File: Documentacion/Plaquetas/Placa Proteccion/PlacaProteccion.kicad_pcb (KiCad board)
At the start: 2 copper layers, 100 x 50 mm, 18 parts, among them J1 POW_IN, J2 POW_OUT, J3 RELAY_CTRL, J4 RELAY_SW, K1 Modulo_Relé, Q1 IRF4905, SW1 ON_SW, SW2 OFF_SW, U1 LM2903, U6 TL431LP

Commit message: Protection PCB footprint update, adjustable zenner ref set, pad resize
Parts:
- added R3: 100k, Resistor_THT:R_Axial_DIN0309_L9.0mm_D3.2mm_P12.70mm_Horizontal, F.Cu at (81.3, 59.5)
- added R4: 100k, Resistor_THT:R_Axial_DIN0309_L9.0mm_D3.2mm_P12.70mm_Horizontal, F.Cu at (81.5, 37.5)
- C1: footprint Capacitor_SMD:C_1206_3216Metric_Pad1.42x1.75mm_HandSolder -> Capacitor_THT:C_Rect_L7.0mm_W2.0mm_P5.00mm
- moved C1 18.5 mm to (73.9, 52.6)
- moved U6 10.4 mm to (85.9, 39.0)
- moved U1 10.0 mm to (100.9, 46.5)
- moved RV1 7.89 mm to (106.9, 41.7)
- moved J3 7.52 mm to (45.1, 62.4)
- moved R2 6.70 mm to (86.3, 53.2)
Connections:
- U6 pad 1: Net-(R2-Pad2) -> Net-(R3-Pad2)
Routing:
- net RELAY_NO: track 171.4 -> 141.9 mm
- net POW_IN-: track 236.5 -> 260.2 mm
- net Net-(R3-Pad2): track 0.00 -> 20.7 mm
- net Net-(D2-Pad1): track 21.3 -> 13.4 mm
- net Net-(J3-Pad3): track 32.8 -> 26.1 mm
- net Net-(R2-Pad2): track 28.2 -> 22.3 mm
- net Net-(RV1-Pad2): track 23.4 -> 26.1 mm

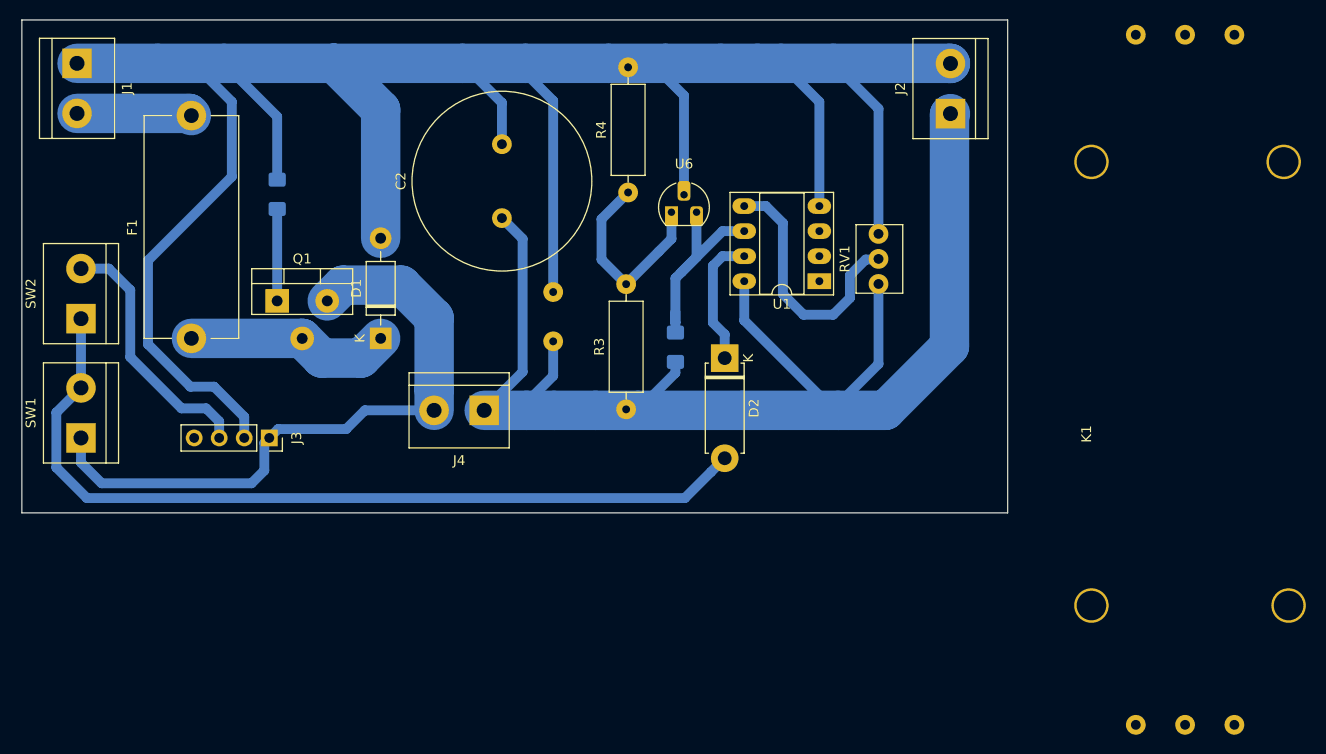
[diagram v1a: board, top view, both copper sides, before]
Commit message: Protection PCB widen tracks, connected unused opamp
This is the final version. It was printed and etched
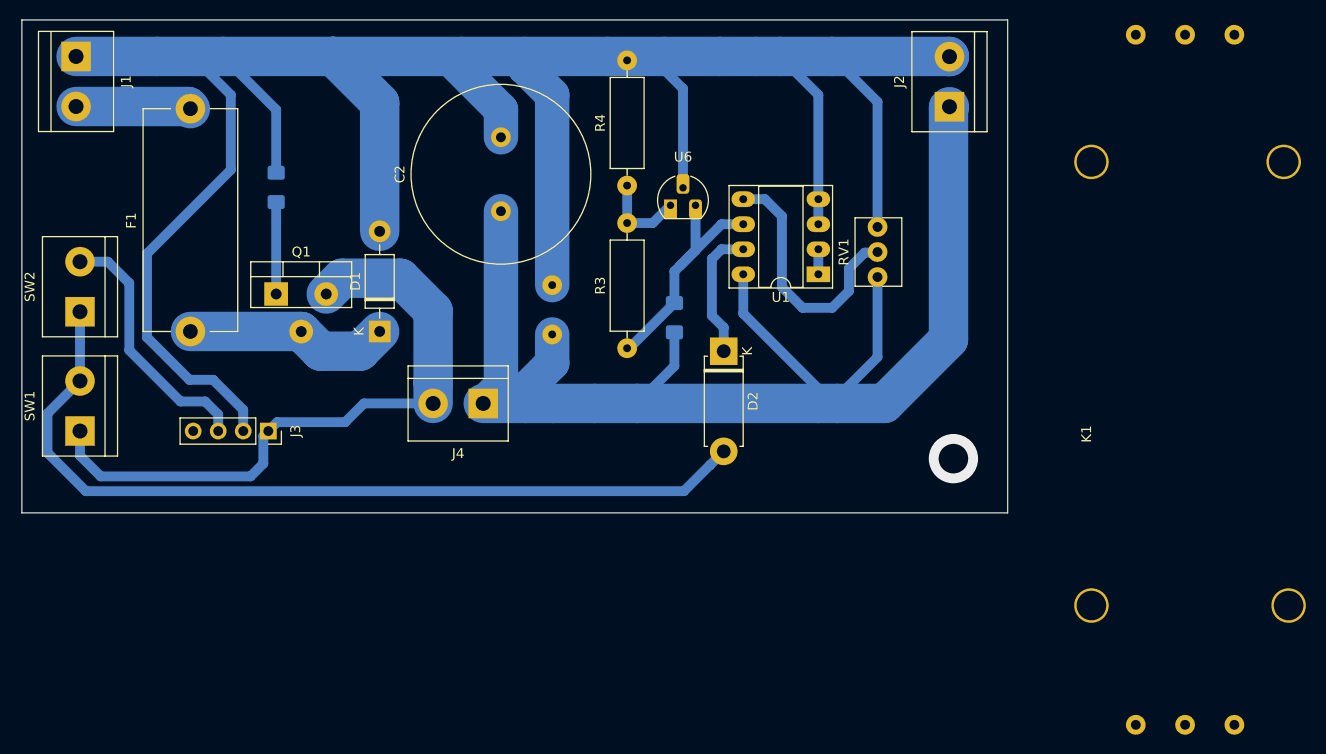
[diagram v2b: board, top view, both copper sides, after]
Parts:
- moved R3 6.20 mm to (81.4, 53.3)
- moved R2 3.00 mm to (86.2, 50.2)
- moved C1 0.71 mm to (73.8, 51.9)
- moved C2 0.71 mm to (68.6, 39.4)
- moved J4 0.71 mm to (66.8, 58.9)
- moved RV1 0.71 mm to (106.8, 41.0)
- moved U1 0.71 mm to (100.8, 45.8)
- moved U6 0.71 mm to (85.8, 38.3)
- moved Q1 0.71 mm to (45.8, 47.8)
- moved R1 0.71 mm to (45.8, 37.0)
- moved R4 0.71 mm to (81.4, 36.8)
- moved J2 0.71 mm to (114.1, 28.8)
- moved J1 0.71 mm to (25.5, 23.7)
- moved D1 0.71 mm to (56.3, 51.6)
- moved F1 0.71 mm to (37.1, 51.6)
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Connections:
- R3 pad 1: RELAY_NO -> Net-(R2-Pad2)
- U1 pad 1: (no net) -> Net-(U1-Pad1)
- U1 pad 2: (no net) -> Net-(U1-Pad1)
- U1 pad 3: (no net) -> POW_IN-
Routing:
- net Net-(R3-Pad2): track 20.7 -> 8.95 mm
- net POW_IN-: track 260.2 -> 266.6 mm
- net Net-(R2-Pad2): track 22.3 -> 25.6 mm
- net Net-(U1-Pad1): track 0.00 -> 2.54 mm
- net RELAY_NO: track 141.9 -> 142.7 mm
- net Net-(D2-Pad2): track 86.9 -> 87.6 mm
- net (no net): vias 0 -> 1

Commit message: Addition of connetors on scheema and PCB
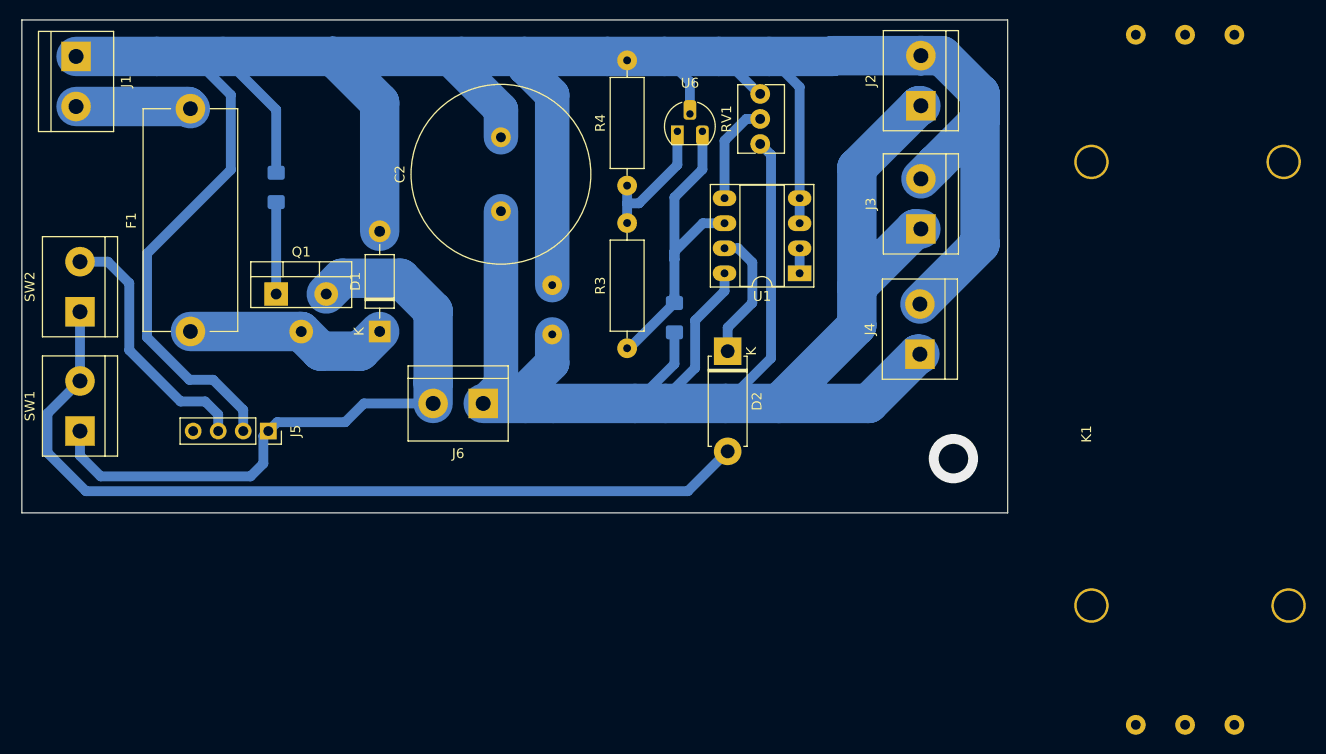
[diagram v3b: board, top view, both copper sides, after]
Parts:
- added J3: POW_OUT, TerminalBlock:TerminalBlock_bornier-2_P5.08mm, F.Cu at (111.2, 41.2)
- added J4: POW_OUT, TerminalBlock:TerminalBlock_bornier-2_P5.08mm, F.Cu at (111.1, 53.9)
- moved RV1 18.0 mm to (94.9, 27.5)
- moved U6 7.53 mm to (86.5, 30.8)
- moved J2 2.90 mm to (111.2, 28.7)
- moved U1 1.90 mm to (98.9, 45.7)
- moved D2 0.40 mm to (91.6, 53.6)
- renumbered J3 to J5, J4 to J6
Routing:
- net RELAY_NO: track 142.7 -> 177.2 mm
- net POW_IN-: track 266.6 -> 285.2 mm
- net Net-(RV1-Pad2): track 26.1 -> 10.4 mm
- net Net-(R2-Pad2): track 25.6 -> 32.4 mm
- net Net-(R3-Pad2): track 8.95 -> 13.9 mm
